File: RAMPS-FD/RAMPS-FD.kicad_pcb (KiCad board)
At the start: 2 copper layers, 100 x 100 mm, 159 parts, among them J1 NET-TIE, K201 S1, K202 S2, K203 S3, K204 S4, M101 LOGO_OSHW, P1 SERIAL1, P101 HB_IN, P102 RESET, P105 12V-AUX, P108 POWER_IN, P2 I2C-1, P201 3 2 1, P202 3 2 1, P203 3 2 1, P204 X, P205 Y, P206 Z1, P207 3 2 1, P208 3 2 1, P209 3 2 1, P210 E2, P211 I2C-0, P212 E1, P213 AUX-4, P214 AUX-2, P215 AUX-3, P216 SERIAL0, P217 E0, P218 D11, P219 EXT_5V, P3 Z2, P301 THERMISTORS, P302 ESTOP, P403 D9, P404 D8, P405 D10, P801 ENDSTOPS, P802 -X+ -Y+ -Z+, P901 D12, P902 D2, Q1 DMN2075, Q101 DMN2075, Q201 IRLB8743PBF, Q202 IRLB8743PBF, Q203 IRLB8743PBF, Q206 IRLB8743PBF, Q901 DMN2075U, Q902 DMN2075U, SW101 RESET, U1 74HCT125, U2 74HCT244, U201 X, U202 Y, U203 Z, U204 E2, U205 E1, U206 E0, U3 LM7812, U4 L7805CV-DG, U601 24C512, U801 74HC4050

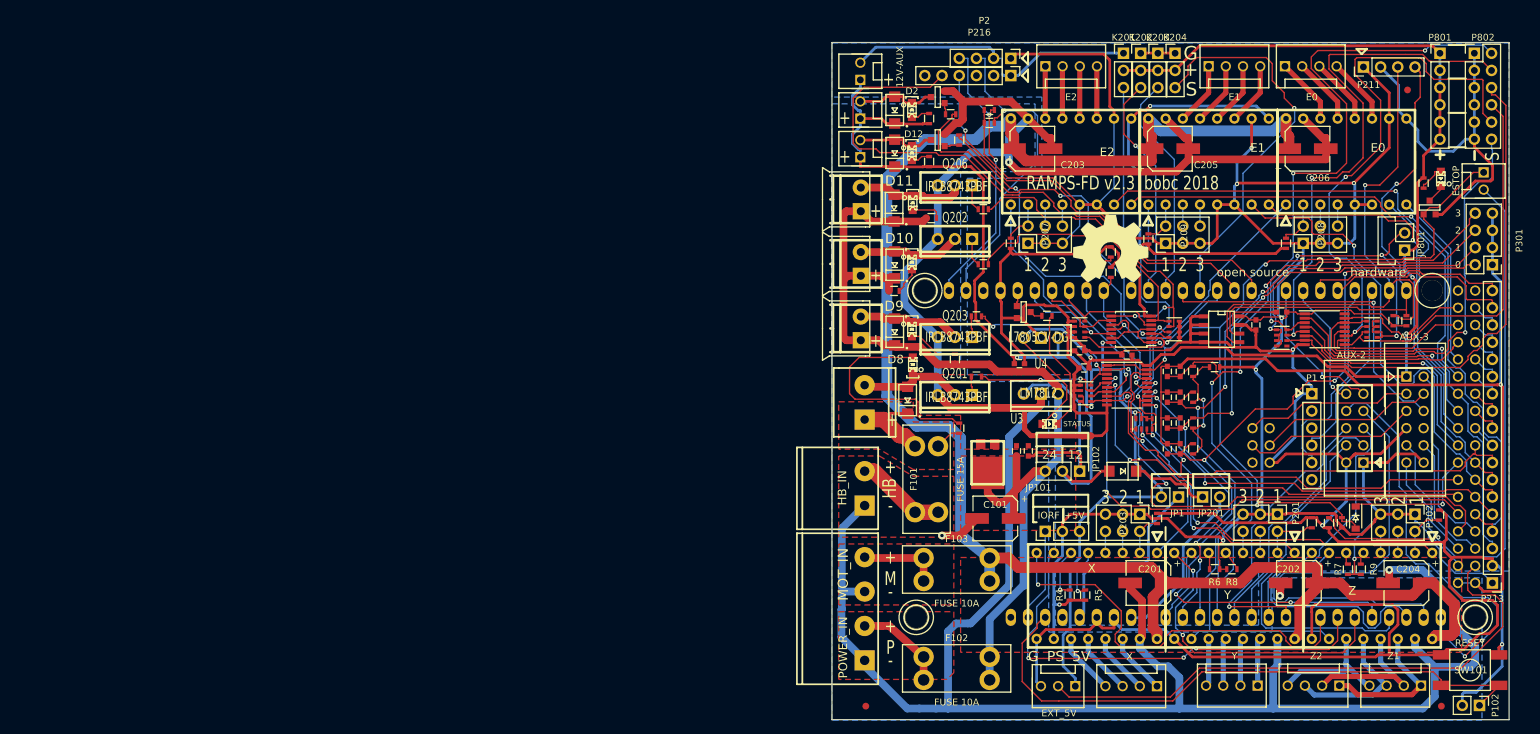
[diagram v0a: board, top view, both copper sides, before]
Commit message: Inital Commit RAMPS FD v2.3. SPI Support for every Driver added.
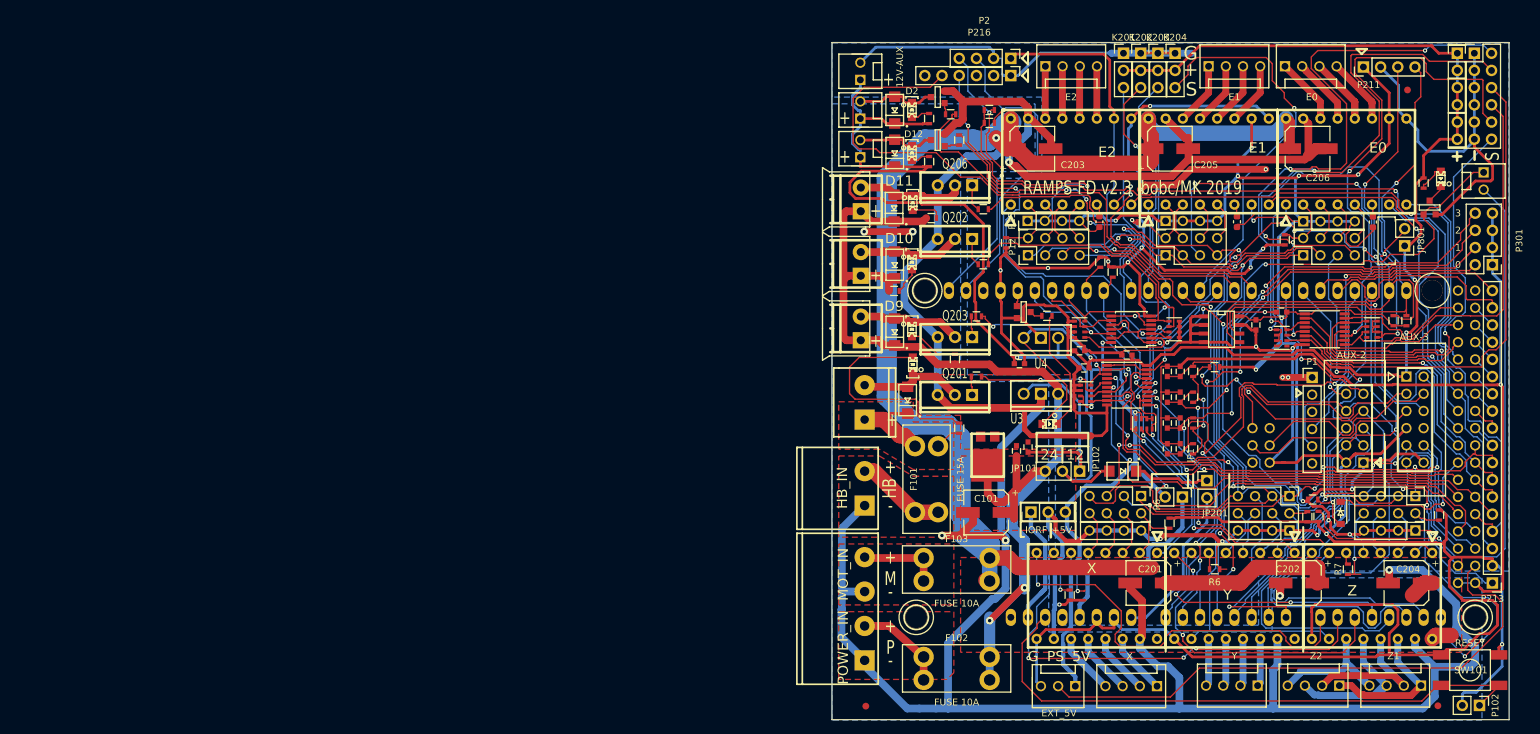
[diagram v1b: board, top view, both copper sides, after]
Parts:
- removed M101: LOGO_OSHW, rmc:OSHW_logo_2
- removed P201, P202, P203, P207, P208, P209: 3 2 1, Pin_Headers:Pin_Header_Straight_2x03_Pitch2.54mm
- removed R5, R8, R9: 10k, Resistors_SMD:R_0603
- added P10: THERMISTORS, Connector_PinHeader_2.54mm:PinHeader_2x04_P2.54mm_Vertical, F.Cu at (101.6, 71.0)
- added P11: THERMISTORS, Connector_PinHeader_2.54mm:PinHeader_2x04_P2.54mm_Vertical, F.Cu at (121.9, 71.0)
- added P12: THERMISTORS, Connector_PinHeader_2.54mm:PinHeader_2x04_P2.54mm_Vertical, F.Cu at (81.3, 71.0)
- added P13: I2C-0, Connector_PinHeader_2.54mm:PinHeader_1x04_P2.54mm_Vertical, F.Cu at (121.9, 66.0)
- added P14: I2C-0, Connector_PinHeader_2.54mm:PinHeader_1x04_P2.54mm_Vertical, F.Cu at (101.6, 65.9)
- added P15: I2C-0, Connector_PinHeader_2.54mm:PinHeader_1x04_P2.54mm_Vertical, F.Cu at (81.2, 65.9)
- added P4: THERMISTORS, Connector_PinHeader_2.54mm:PinHeader_2x04_P2.54mm_Vertical, F.Cu at (119.9, 106.6)
- added P5: THERMISTORS, Connector_PinHeader_2.54mm:PinHeader_2x04_P2.54mm_Vertical, F.Cu at (138.5, 106.6)
- added P6: THERMISTORS, Connector_PinHeader_2.54mm:PinHeader_2x04_P2.54mm_Vertical, F.Cu at (98.0, 106.5)
- added P7: I2C-0, Connector_PinHeader_2.54mm:PinHeader_1x04_P2.54mm_Vertical, F.Cu at (98.0, 111.6)
- added P8: I2C-0, Connector_PinHeader_2.54mm:PinHeader_1x04_P2.54mm_Vertical, F.Cu at (119.9, 111.6)
- added P9: I2C-0, Connector_PinHeader_2.54mm:PinHeader_1x04_P2.54mm_Vertical, F.Cu at (138.5, 111.6)
- added R10: 10k, Resistor_SMD:R_0603_1608Metric, F.Cu at (91.8, 66.0)
- added R12: 10k, Resistor_SMD:R_0603_1608Metric, F.Cu at (112.1, 66.0)
- added R14: 10k, Resistor_SMD:R_0603_1608Metric, F.Cu at (132.2, 66.1)
- U3: value LM7812 -> R-78E12-0.5
- moved R304 5.51 mm to (123.3, 107.1), turned to 0 degrees
- moved JP101 3.54 mm to (81.7, 108.9)
- moved R208 2.63 mm to (98.2, 66.1), turned to 180 degrees
- moved P801 2.57 mm to (144.7, 41.1)
- moved JP1 2.50 mm to (107.7, 104.3), turned to 0 degrees
- moved P1 2.41 mm to (123.2, 89.0)
- moved D301 2.33 mm to (127.4, 109.0)
- moved R402 2.16 mm to (91.9, 72.0)
- moved R202 1.97 mm to (102.2, 110.6)
- moved R305 1.81 mm to (124.2, 109.6)
- moved C101 1.61 mm to (75.1, 109.0)
- moved R203 1.11 mm to (122.5, 109.6), turned to 270 degrees
- moved D102 1.10 mm to (75.3, 100.5)
- moved R207 0.70 mm to (78.0, 69.2)
- moved JP801 0.63 mm to (136.9, 69.6)
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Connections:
- P1 pad 2: (no net) -> Net-(P1-Pad2)
- P1 pad 3: (no net) -> Net-(P1-Pad3)
- P1 pad 6: (no net) -> Net-(P1-Pad6)
- P215 pad 8: (no net) -> Net-(P215-Pad8)
- P216 pad 2: (no net) -> Net-(P216-Pad2)
- P216 pad 3: (no net) -> Net-(P216-Pad3)
- P216 pad 6: (no net) -> Net-(P216-Pad6)
- RP801 pad 1: (no net) -> Net-(RP801-Pad1)
- RP802 pad 4: (no net) -> Net-(RP802-Pad4)
- SHIELD101 pad 3V3: (no net) -> +3V3
- SHIELD101 pad 5V_4: (no net) -> Net-(SHIELD101-Pad5V_4)
- SHIELD101 pad 5V_5: (no net) -> Net-(SHIELD101-Pad5V_5)
- SHIELD101 pad 5V_6: (no net) -> Net-(SHIELD101-Pad5V_6)
- SHIELD101 pad AREF: (no net) -> Net-(SHIELD101-PadAREF)
- SHIELD101 pad RST2: (no net) -> Net-(SHIELD101-PadRST2)
- U201 pad 4: STEP_X_CS -> Net-(P6-Pad6)
- U202 pad 4: STEP_Y_CS -> Net-(P4-Pad6)
- U203 pad 4: STEP_Z_CS -> Net-(P5-Pad6)
- U204 pad 5: +V_LOGIC -> Net-(P12-Pad8)
- U204 pad 6: +V_LOGIC -> Net-(R10-Pad2)
- U205 pad 5: +V_LOGIC -> Net-(P10-Pad8)
- U205 pad 6: +V_LOGIC -> Net-(R12-Pad2)
- U206 pad 5: +V_LOGIC -> Net-(P11-Pad8)
- U206 pad 6: +V_LOGIC -> Net-(R14-Pad2)
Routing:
- net D50-MISO: track 18.4 -> 174.1 mm, vias 0 -> 5
- net D51-MOSI: track 19.3 -> 161.8 mm, vias 0 -> 6
- net D52-SCK: track 18.4 -> 159.3 mm, vias 0 -> 5
- net A5: track 31.2 -> 117.4 mm, vias 0 -> 3
- net AD14: track 68.5 -> 133.9 mm, vias 0 -> 6
- net AD15: track 61.4 -> 116.8 mm, vias 2 -> 6
- net +V_LOGIC: track 436.7 -> 480.6 mm, vias 8 -> 18
- net GND: track 604.7 -> 643.4 mm, vias 6 -> 18
- net A4: track 37.4 -> 74.3 mm, vias 0 -> 2
- net Net-(JP801-Pad2): track 57.5 -> 82.0 mm, vias 4 -> 3
- net +V_MOTOR: track 253.1 -> 231.9 mm, vias 0 -> 1
- net +12P: track 119.3 -> 138.7 mm
- net /Stepper Drivers/Z-1A: track 21.3 -> 36.9 mm
- net +5V: track 271.6 -> 287.0 mm
- net MOT_GND: track 430.1 -> 445.3 mm, vias 4 -> 7
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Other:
- board text added: "RAMPS-FD v2.3 bobc/MK 2019"
- board text removed: "RAMPS-FD v2.3 bobc 2018"

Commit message: Added UART for Communication with TMC2209 Drivers, improved inverse-polarity protection, added Driver Protection. Two Layer Design
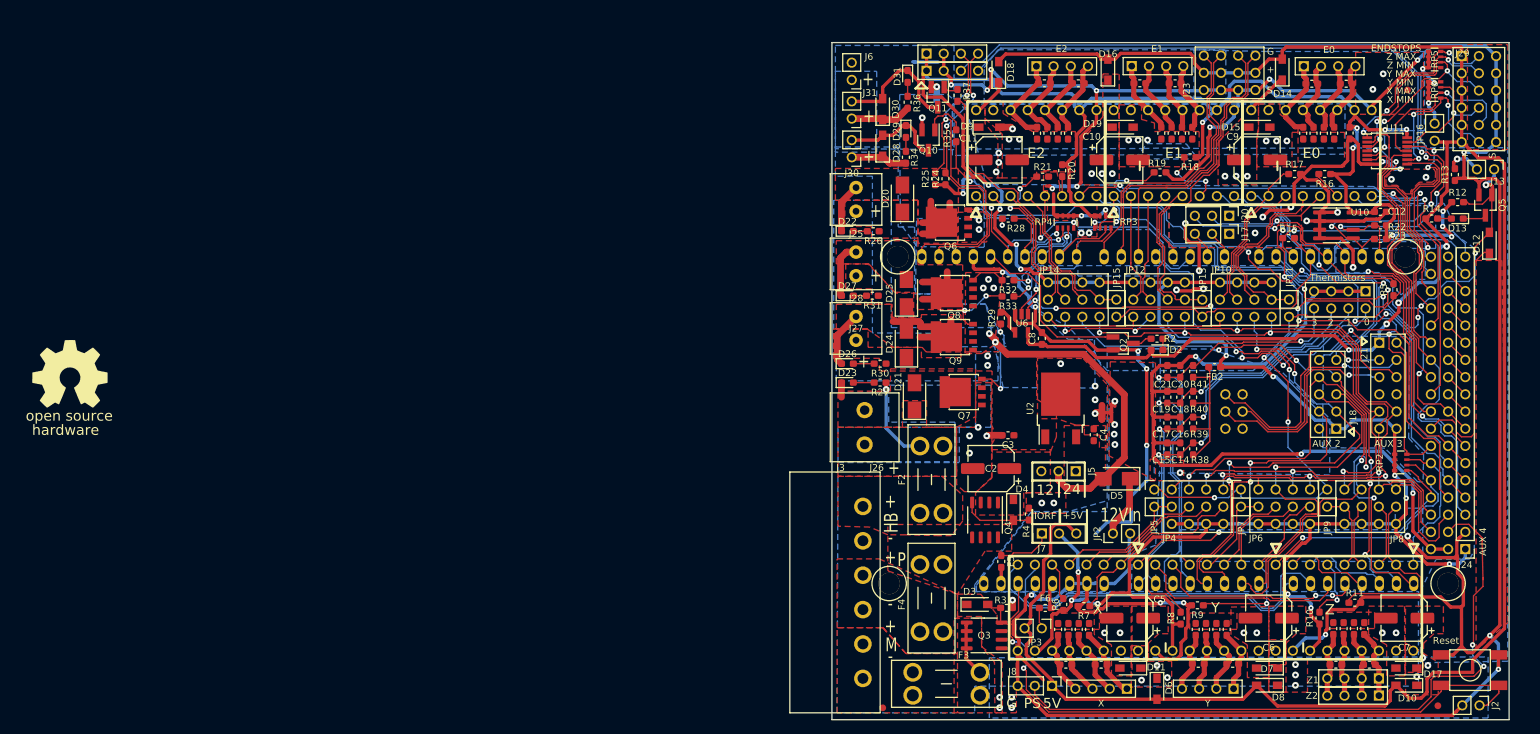
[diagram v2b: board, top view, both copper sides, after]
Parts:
- removed C102: 100n 50V, Capacitors_SMD:C_0603
- removed the C2 at (89.5, 87.6)
- removed C203: 100u 35V, Capacitors_SMD:CP_Elec_6.3x7.7
- removed D101: STATUS, rmc:LED-0805_GREEN
- removed D102: V10P10, rmc:TO277A_RMC
- removed D203, D902: LED RED, rmc:LED-0805_RED
- removed F102, F103: FUSE 10A, rmc:Keystone_3568
- removed J1: NET-TIE, rmc:TIE-1MM
- removed JP102: VSEL, Pin_Headers:Pin_Header_Straight_1x03_Pitch2.54mm
- removed JP201: 5V_SEL, Pin_Headers:Pin_Header_Straight_1x02_Pitch2.54mm
- removed K201: S1, Pin_Headers:Pin_Header_Straight_1x03_Pitch2.54mm
- removed K202: S2, Pin_Headers:Pin_Header_Straight_1x03_Pitch2.54mm
- removed K203: S3, Pin_Headers:Pin_Header_Straight_1x03_Pitch2.54mm
- removed K204: S4, Pin_Headers:Pin_Header_Straight_1x03_Pitch2.54mm
- removed P1: SERIAL1, Pin_Headers:Pin_Header_Straight_1x06_Pitch2.54mm
- removed P10, P11, P12, P4, P5, P6: THERMISTORS, Connector_PinHeader_2.54mm:PinHeader_2x04_P2.54mm_Vertical
- removed P101: HB_IN, w_conn_screw:mstba_2,5%2f2-g-5,08
- removed P108: POWER_IN, w_conn_screw:mstba_2,5%2f4-g-5,08
- removed P13, P14, P15, P7, P8, P9: I2C-0, Connector_PinHeader_2.54mm:PinHeader_1x04_P2.54mm_Vertical
- removed P204: X, rmc:CONN_KK_2.54_4W
- removed P216: SERIAL0, Pin_Headers:Pin_Header_Straight_1x06_Pitch2.54mm
- removed P301: THERMISTORS, Pin_Headers:Pin_Header_Straight_2x04_Pitch2.54mm
- removed P801: ENDSTOPS, Pin_Headers:Pin_Header_Straight_1x06_Pitch2.54mm
- removed P802: -X+ -Y+ -Z+, Pin_Headers:Pin_Header_Straight_2x06_Pitch2.54mm
- removed R101: 330R, Resistors_SMD:R_0603
- removed R219, R905, R906: 1k, Resistors_SMD:R_0603
- removed R401, R402: 10k, Resistors_SMD:R_0603
- removed the RP2 at (98.4, 95.9)
- removed SHIELD101: ARDUINO_DUE_SHIELD, rmc:ARDUINO_MEGA_DUE_SHIELD_FOOTPRINT_RMC
- removed the U2 at (95.9, 90.2)
- removed U204: E2, rmc:POLOLU
- removed U206: E0, rmc:POLOLU
- removed the U3 at (83.2, 91.4)
- removed the U4 at (83.2, 83.2)
- removed U601: 24C512, libcms:SO8E
- removed U801: 74HC4050, Housings_SSOP:TSSOP-16_4.4x5mm_Pitch0.65mm
- added D10: DS110W, RAMPS-FD:D_SOD-123F, F.Cu at (137.2, 134.5)
- added D11: SMF36CA, RAMPS-FD:D_SOD-123F, F.Cu at (96.4, 132.0)
- added D14: DS110W, RAMPS-FD:D_SOD-123F, F.Cu at (118.8, 43.6)
- added D15: SMF36CA, RAMPS-FD:D_SOD-123F, F.Cu at (115.4, 52.1)
- added D16: DS110W, RAMPS-FD:D_SOD-123F, F.Cu at (93.1, 43.6)
- added D17: SMF36CA, RAMPS-FD:D_SOD-123F, F.Cu at (137.2, 132.0)
- added D18: DS110W, RAMPS-FD:D_SOD-123F, F.Cu at (77.0, 43.9)
- added D19: SMF36CA, RAMPS-FD:D_SOD-123F, F.Cu at (95.2, 52.1)
- added D2: LED_0603_GREEN, RAMPS-FD:LED_0603, F.Cu at (100.3, 85.0)
- added D26: LED_0603_RED, RAMPS-FD:LED_0603, F.Cu at (54.6, 87.0)
- added D3: KDZVTR11B, RAMPS-FD:D_SOD-123F, F.Cu at (73.8, 122.6)
- added D31: LED_0603_RED, RAMPS-FD:LED_0603, F.Cu at (63.5, 44.6)
- added D4: KDZVTR11B, RAMPS-FD:D_SOD-123F, F.Cu at (79.1, 108.6)
- added D6: DS110W, RAMPS-FD:D_SOD-123F, F.Cu at (100.3, 135.0)
- added D7: SMF36CA, RAMPS-FD:D_SOD-123F, F.Cu at (116.6, 132.0)
- added D8: DS110W, RAMPS-FD:D_SOD-123F, F.Cu at (116.6, 134.5)
- added D9: SMF36CA, RAMPS-FD:D_SOD-123F, F.Cu at (75.6, 52.1)
- added F3: Keystone_3568, RAMPS-FD:Fuseholder_Blade_Mini_Keystone_3568, F.Cu at (64.3, 132.6)
- added F4: Keystone_3568, RAMPS-FD:Fuseholder_Blade_Mini_Keystone_3568, F.Cu at (65.3, 126.6)
- added F5: FUSE_750mA_0603, RAMPS-FD:R_0603, F.Cu at (77.3, 116.2)
- added F6: FUSE_750mA_0603, RAMPS-FD:R_0603, F.Cu at (83.8, 123.1)
- added J17: 1x3PinHeader, RAMPS-FD:PinHeader_1x03_P2.54mm_Vertical, F.Cu at (111.0, 67.8)
- added J20: 1x3PinHeader, RAMPS-FD:PinHeader_1x03_P2.54mm_Vertical, F.Cu at (111.0, 65.2)
- added J23: 3x4PinHeader, RAMPS-FD:4x3_2.54mm_Header, F.Cu at (107.2, 46.6)
- added J29: 3x6PinHeader, RAMPS-FD:6x3_2.54mm_Header, F.Cu at (145.3, 41.6)
- added J3: 6_PinScrewPlugableTerminal_P508, RAMPS-FD:6x1_P508_RA, F.Cu at (56.9, 120.8)
- added J32: 2x4PinHeader_2.54mm, RAMPS-FD:pin_header_2.54mm_2x4, F.Cu at (127.3, 77.6)
- added J5: 1x3JumperArray, RAMPS-FD:PinHeader_1x03_P2.54mm_Vertical, F.Cu at (88.3, 102.9)
- added J9: 1x4PinHeader, RAMPS-FD:pin_header_2.54mm_1x4, F.Cu at (92.1, 135.0)
- added JP10: 4x3JumperArray, RAMPS-FD:4x3_2.54mm_Header, F.Cu at (109.6, 80.1)
- added JP11: 1x2JumperArray, RAMPS-FD:PinHeader_1x02_P2.54mm_Vertical, F.Cu at (119.8, 80.1)
- added JP12: 4x3JumperArray, RAMPS-FD:4x3_2.54mm_Header, F.Cu at (96.8, 80.1)
- added JP13: 1x2JumperArray, RAMPS-FD:PinHeader_1x02_P2.54mm_Vertical, F.Cu at (107.0, 80.1)
- added JP14: 4x3JumperArray, RAMPS-FD:4x3_2.54mm_Header, F.Cu at (84.2, 80.1)
- added JP15: 1x2JumperArray, RAMPS-FD:PinHeader_1x02_P2.54mm_Vertical, F.Cu at (94.3, 80.1)
- added JP3: 1x2JumperArray, RAMPS-FD:PinHeader_1x02_P2.54mm_Vertical, F.Cu at (83.3, 126.1)
- added JP4: 4x3JumperArray, RAMPS-FD:4x3_2.54mm_Header, F.Cu at (110.1, 105.6)
- added JP5: 1x2JumperArray, RAMPS-FD:PinHeader_1x02_P2.54mm_Vertical, F.Cu at (99.9, 105.6)
- added JP6: 4x3JumperArray, RAMPS-FD:4x3_2.54mm_Header, F.Cu at (122.9, 105.6)
- added JP7: 1x2JumperArray, RAMPS-FD:PinHeader_1x02_P2.54mm_Vertical, F.Cu at (112.7, 105.6)
- added JP8: 4x3JumperArray, RAMPS-FD:4x3_2.54mm_Header, F.Cu at (135.6, 105.6)
- added JP9: 1x2JumperArray, RAMPS-FD:PinHeader_1x02_P2.54mm_Vertical, F.Cu at (125.5, 105.6)
- added M2: LOGO_OSHW, RAMPS-FD:OSHW_logo_2, F.Cu at (-60.2, 88.5)
- added NT1: NetTie-2_SMD_Pad0.5mm, NetTie:NetTie-2_SMD_Pad0.5mm, F.Cu at (93.1, 94.2)
- added Q3: TDM3415, RAMPS-FD:SO-8_3.9x4.9mm_P1.27mm, F.Cu at (74.8, 127.1)
- added Q4: TDM3415, RAMPS-FD:SO-8_3.9x4.9mm_P1.27mm, F.Cu at (74.9, 110.1)
- added R14: 330R, RAMPS-FD:R_0603, F.Cu at (140.9, 65.6)
- added R15: 1k, RAMPS-FD:R_0603, F.Cu at (119.8, 68.5)
- added R2: 330R, RAMPS-FD:R_0603, F.Cu at (100.3, 83.3)
- added R27: 1k, RAMPS-FD:R_0603, F.Cu at (59.4, 89.8)
- added R34: 1k, RAMPS-FD:R_0603, F.Cu at (63.2, 56.5)
- added R36: 1k, RAMPS-FD:R_0603, F.Cu at (63.5, 48.4)
- added R5: 1k, RAMPS-FD:R_0603, F.Cu at (135.3, 76.1)
- added R6: 10k, RAMPS-FD:R_0603, F.Cu at (86.5, 122.6)
- added REF**: OSHW-Logo2_9.8x8mm_SilkScreen, Symbol:OSHW-Logo2_9.8x8mm_SilkScreen, B.Cu at (81.9, 88.5)
- added SHIELD2: ARDUINO_DUE_SHIELD, RAMPS-FD:ARDUINO_MEGA_DUE_SHIELD_FOOTPRINT_RMC, F.Cu at (46.8, 122.0)
- added U10: 24C512, RAMPS-FD:SOIC-8_3.9x4.9mm_P1.27mm, F.Cu at (126.8, 66.6)
- added U11: MC74LCX07, RAMPS-FD:TSSOP-14_4.4x5mm_P0.65mm, F.Cu at (134.3, 55.6)
- added U6: SN74LV1T125, RAMPS-FD:SOT-23-5, F.Cu at (80.3, 81.0)
- added U7: Pololu, RAMPS-FD:POLOLU, F.Cu at (123.1, 55.9)
- added U9: Pololu, RAMPS-FD:POLOLU, F.Cu at (82.5, 55.9)
- added VR10: 33V, RAMPS-FD:R_0603, F.Cu at (107.6, 126.2)
- added VR11: 33V, RAMPS-FD:R_0603, F.Cu at (106.0, 126.2)
- added VR12: 33V, RAMPS-FD:R_0603, F.Cu at (111.5, 131.3)
- added VR13: 33V, RAMPS-FD:R_0603, F.Cu at (106.4, 131.3)
- added VR14: 33V, RAMPS-FD:R_0603, F.Cu at (129.4, 126.1)
- added VR15: 33V, RAMPS-FD:R_0603, F.Cu at (130.9, 126.1)
- added VR16: 33V, RAMPS-FD:R_0603, F.Cu at (127.9, 126.1)
- added VR17: 33V, RAMPS-FD:R_0603, F.Cu at (126.4, 126.1)
- added VR18: 33V, RAMPS-FD:R_0603, F.Cu at (131.7, 131.4)
- added VR19: 33V, RAMPS-FD:R_0603, F.Cu at (126.7, 131.4)
- added VR2: 33V, RAMPS-FD:R_0603, F.Cu at (92.1, 131.4)
- added VR20: 33V, RAMPS-FD:R_0603, F.Cu at (123.2, 45.7)
- added VR21: 33V, RAMPS-FD:R_0603, F.Cu at (128.3, 45.7)
- added VR22: 33V, RAMPS-FD:R_0603, F.Cu at (123.4, 53.0)
- added VR23: 33V, RAMPS-FD:R_0603, F.Cu at (121.9, 53.0)
- added VR24: 33V, RAMPS-FD:R_0603, F.Cu at (125.0, 53.0)
- added VR25: 33V, RAMPS-FD:R_0603, F.Cu at (126.5, 53.0)
- added VR26: 33V, RAMPS-FD:R_0603, F.Cu at (97.8, 45.6)
- added VR27: 33V, RAMPS-FD:R_0603, F.Cu at (103.0, 45.6)
- added VR28: 33V, RAMPS-FD:R_0603, F.Cu at (101.0, 53.0)
- added VR29: 33V, RAMPS-FD:R_0603, F.Cu at (102.5, 53.0)
- added VR3: 33V, RAMPS-FD:R_0603, F.Cu at (86.9, 131.4)
- added VR30: 33V, RAMPS-FD:R_0603, F.Cu at (104.0, 53.0)
- added VR31: 33V, RAMPS-FD:R_0603, F.Cu at (105.5, 53.0)
- added VR32: 33V, RAMPS-FD:R_0603, F.Cu at (82.6, 53.0)
- added VR33: 33V, RAMPS-FD:R_0603, F.Cu at (84.1, 53.0)
- added VR34: 33V, RAMPS-FD:R_0603, F.Cu at (85.7, 53.0)
- added VR35: 33V, RAMPS-FD:R_0603, F.Cu at (87.2, 53.0)
- added VR36: 33V, RAMPS-FD:R_0603, F.Cu at (83.7, 45.6)
- added VR37: 33V, RAMPS-FD:R_0603, F.Cu at (88.7, 45.6)
- added VR4: 33V, RAMPS-FD:R_0603, F.Cu at (88.8, 126.2)
- added VR5: 33V, RAMPS-FD:R_0603, F.Cu at (90.3, 126.2)
- added VR6: 33V, RAMPS-FD:R_0603, F.Cu at (87.2, 126.2)
- added VR7: 33V, RAMPS-FD:R_0603, F.Cu at (85.7, 126.2)
- added VR8: 33V, RAMPS-FD:R_0603, F.Cu at (109.1, 126.2)
- added VR9: 33V, RAMPS-FD:R_0603, F.Cu at (110.6, 126.2)
- C10: renamed from C205; value 100u 35V -> 100u_35V; footprint Capacitors_SMD:CP_Elec_6.3x7.7 -> RAMPS-FD:CP_Elec_6.3x7.7
- C11: renamed from C204; value 100u 35V -> 100u_35V; footprint Capacitors_SMD:CP_Elec_6.3x7.7 -> RAMPS-FD:CP_Elec_6.3x7.7
- C12: renamed from C601; footprint Capacitors_SMD:C_0603 -> RAMPS-FD:C_0603
- C13: renamed from C305; footprint Capacitors_SMD:C_0603 -> RAMPS-FD:C_0603
- C14: renamed from C504; footprint Capacitors_SMD:C_0603 -> RAMPS-FD:C_0603
- C15: renamed from C301; footprint Capacitors_SMD:C_0603 -> RAMPS-FD:C_0603
- C16: renamed from C505; footprint Capacitors_SMD:C_0603 -> RAMPS-FD:C_0603
- C17: renamed from C302; footprint Capacitors_SMD:C_0603 -> RAMPS-FD:C_0603
- C18: renamed from C503; footprint Capacitors_SMD:C_0603 -> RAMPS-FD:C_0603
- C19: renamed from C303; footprint Capacitors_SMD:C_0603 -> RAMPS-FD:C_0603
- C2: renamed from C101; value 100u 35V -> 100u_35V; footprint Capacitors_SMD:CP_Elec_6.3x7.7 -> RAMPS-FD:CP_Elec_6.3x7.7
- C20: renamed from C502; footprint Capacitors_SMD:C_0603 -> RAMPS-FD:C_0603
- C21: renamed from C501; footprint Capacitors_SMD:C_0603 -> RAMPS-FD:C_0603
- C3: footprint Capacitors_SMD:C_0603 -> RAMPS-FD:C_0603
- C4: renamed from C207; footprint Capacitors_SMD:C_0603 -> RAMPS-FD:C_0603
- C5: renamed from C201; value 100u 35V -> 100u_35V; footprint Capacitors_SMD:CP_Elec_6.3x7.7 -> RAMPS-FD:CP_Elec_6.3x7.7
- C6: renamed from C202; value 100u 35V -> 100u_35V; footprint Capacitors_SMD:CP_Elec_6.3x7.7 -> RAMPS-FD:CP_Elec_6.3x7.7
- C7: renamed from C4; value 100n -> 100u_35V; footprint Capacitors_SMD:C_0603 -> RAMPS-FD:CP_Elec_6.3x7.7
- C8: renamed from C1; footprint Capacitors_SMD:C_0603 -> RAMPS-FD:C_0603
- C9: renamed from C206; value 100u 35V -> 100u_35V; footprint Capacitors_SMD:CP_Elec_6.3x7.7 -> RAMPS-FD:CP_Elec_6.3x7.7
- D12: renamed from D301; value 1N4148 -> 2CZ4007; footprint Diodes_SMD:SOD-123 -> RAMPS-FD:D_SOD-123F
- D13: renamed from D1; value ESTOP -> LED_0603_GREEN; footprint rmc:LED-0805_GREEN -> RAMPS-FD:LED_0603
- D20: renamed from D403; value ES1F -> MRA4003T3G; footprint rmc:DO-214AC -> RAMPS-FD:D_SMA
- D21: renamed from D404; value ES1F -> MRA4003T3G; footprint rmc:DO-214AC -> RAMPS-FD:D_SMA
- D22: renamed from D204; value LED RED -> LED_0603_RED; footprint rmc:LED-0805_RED -> RAMPS-FD:LED_0603
- D23: renamed from D201; value LED RED -> LED_0603_RED; footprint rmc:LED-0805_RED -> RAMPS-FD:LED_0603
- D24: renamed from D401; value ES1F -> MRA4003T3G; footprint rmc:DO-214AC -> RAMPS-FD:D_SMA
- D25: renamed from D402; value ES1F -> MRA4003T3G; footprint rmc:DO-214AC -> RAMPS-FD:D_SMA
- D27: renamed from D202; value LED RED -> LED_0603_RED; footprint rmc:LED-0805_RED -> RAMPS-FD:LED_0603
- D28: renamed from D903; value ES1F -> 2CZ4007; footprint rmc:DO-214AC -> RAMPS-FD:D_SOD-123F
- D29: renamed from D901; value LED RED -> LED_0603_RED; footprint rmc:LED-0805_RED -> RAMPS-FD:LED_0603
- D30: renamed from D904; value ES1F -> 2CZ4007; footprint rmc:DO-214AC -> RAMPS-FD:D_SOD-123F
- D5: renamed from D103; value ES1F -> MRA4003T3G; footprint rmc:DO-214AC -> RAMPS-FD:D_SMA
- F2: renamed from F101; value FUSE 15A -> Keystone_3568; footprint rmc:Keystone_3568 -> RAMPS-FD:Fuseholder_Blade_Mini_Keystone_3568
- FB2: renamed from L1; value FB -> FB0603; footprint Resistors_SMD:R_0603 -> RAMPS-FD:R_0603
- FID2: renamed from FID1; footprint Fiducials:Fiducial_1mm_Dia_2.54mm_Outer_CopperTop -> RAMPS-FD:Fiducial_1mm_Mask2mm
- FID3: renamed from FID2; footprint Fiducials:Fiducial_1mm_Dia_2.54mm_Outer_CopperTop -> RAMPS-FD:Fiducial_1mm_Mask2mm
- FID4: renamed from FID3; footprint Fiducials:Fiducial_1mm_Dia_2.54mm_Outer_CopperTop -> RAMPS-FD:Fiducial_1mm_Mask2mm
- J10: renamed from P205; value Y -> 1x4PinHeader; footprint rmc:CONN_KK_2.54_4W -> RAMPS-FD:pin_header_2.54mm_1x4
- J11: renamed from P206; value Z1 -> 1x4PinHeader; footprint rmc:CONN_KK_2.54_4W -> RAMPS-FD:pin_header_2.54mm_1x4
- J12: renamed from P3; value Z2 -> 1x4PinHeader; footprint rmc:CONN_KK_2.54_4W -> RAMPS-FD:pin_header_2.54mm_1x4
- J13: renamed from P302; value ESTOP -> 2x1PinHeader; footprint rmc:CONN_KK_2.54_2W -> RAMPS-FD:PinHeader_1x02_P2.54mm_Vertical
- J14: renamed from P217; value E0 -> 1x4PinHeader; footprint rmc:CONN_KK_2.54_4W -> RAMPS-FD:pin_header_2.54mm_1x4
- J15: renamed from P212; value E1 -> 1x4PinHeader; footprint rmc:CONN_KK_2.54_4W -> RAMPS-FD:pin_header_2.54mm_1x4
- J16: renamed from P210; value E2 -> 1x4PinHeader; footprint rmc:CONN_KK_2.54_4W -> RAMPS-FD:pin_header_2.54mm_1x4
- J18: renamed from P214; value AUX-2 -> 2x5PinHeader; footprint rmc:PIN_ARRAY_5x2_RMC -> RAMPS-FD:pin_header_2.54mm_2x5
- J19: renamed from P211; value I2C-0 -> 1x4PinHeader; footprint Pin_Headers:Pin_Header_Straight_1x04_Pitch2.54mm -> RAMPS-FD:pin_header_2.54mm_1x4
- J2: renamed from P102; value RESET -> 2x1PinHeader; footprint Pin_Headers:Pin_Header_Straight_1x02_Pitch2.54mm -> RAMPS-FD:PinHeader_1x02_P2.54mm_Vertical
- J21: renamed from P215; value AUX-3 -> 2x6PinHeader; footprint rmc:PIN_ARRAY_6x2_RMC -> RAMPS-FD:pin_header_2.54mm_2x6
- J22: renamed from P2; value I2C-1 -> 1x4PinHeader; footprint Pin_Headers:Pin_Header_Straight_1x04_Pitch2.54mm -> RAMPS-FD:pin_header_2.54mm_1x4
- J24: renamed from P213; value AUX-4 -> 1x18PinHeader; footprint Pin_Headers:Pin_Header_Straight_1x18_Pitch2.54mm -> RAMPS-FD:PinHeader_1x18_P2.54mm_Vertical
- J25: renamed from P218; value D11 -> 2_PinScrewTerminal_P350; footprint rmc:RMC-pt_1,5-2-3,5-h -> RAMPS-FD:2x1_P350
- J26: renamed from P404; value D8 -> 2_PinScrewTerminal_P508; footprint w_conn_screw:mors_2p -> RAMPS-FD:2x1_P508
- J27: renamed from P403; value D9 -> 2_PinScrewTerminal_P350; footprint rmc:RMC-pt_1,5-2-3,5-h -> RAMPS-FD:2x1_P350
- J28: renamed from P405; value D10 -> 2_PinScrewTerminal_P350; footprint rmc:RMC-pt_1,5-2-3,5-h -> RAMPS-FD:2x1_P350
- J30: renamed from P901; value D12 -> 2x1PinHeader; footprint rmc:CONN_KK_2.54_2W -> RAMPS-FD:PinHeader_1x02_P2.54mm_Vertical
- J31: renamed from P902; value D2 -> 2x1PinHeader; footprint rmc:CONN_KK_2.54_2W -> RAMPS-FD:PinHeader_1x02_P2.54mm_Vertical
- J6: renamed from P105; value 12V-AUX -> 2x1PinHeader; footprint rmc:CONN_KK_2.54_2W -> RAMPS-FD:PinHeader_1x02_P2.54mm_Vertical
- J7: renamed from JP101; value VLOG -> 1x3JumperArray; footprint Pin_Headers:Pin_Header_Straight_1x03_Pitch2.54mm -> RAMPS-FD:PinHeader_1x03_P2.54mm_Vertical
- J8: renamed from P219; value EXT_5V -> 1x3PinHeader; footprint rmc:CONN_KK_2.54_3W -> RAMPS-FD:PinHeader_1x03_P2.54mm_Vertical
- JP16: renamed from JP801; value PULLUPS -> 1x2JumperArray; footprint Pin_Headers:Pin_Header_Straight_1x02_Pitch2.54mm -> RAMPS-FD:PinHeader_1x02_P2.54mm_Vertical
- JP2: renamed from JP1; value VIN -> 1x2JumperArray; footprint Pin_Headers:Pin_Header_Straight_1x02_Pitch2.54mm -> RAMPS-FD:PinHeader_1x02_P2.54mm_Vertical
- Q10: renamed from Q901; value DMN2075U -> NCE3416; footprint libcms:SOT23GDS -> RAMPS-FD:SOT-23
- Q11: renamed from Q902; value DMN2075U -> NCE3416; footprint libcms:SOT23GDS -> RAMPS-FD:SOT-23
- Q2: renamed from Q101; value DMN2075 -> NCE3416; footprint libcms:SOT23GDS -> RAMPS-FD:SOT-23
- Q5: renamed from Q1; value DMN2075 -> NCE3416; footprint libcms:SOT23GDS -> RAMPS-FD:SOT-23
- Q6: renamed from Q206; value IRLB8743PBF -> PSMN7R5-60YLX; footprint rmc:TO-220AB_IRF2804_RMC -> RAMPS-FD:LFPAK56
- Q7: renamed from Q201; value IRLB8743PBF -> PSMN1R8-40YLC; footprint rmc:TO-220AB_IRF2804_RMC -> RAMPS-FD:LFPAK56
- Q8: renamed from Q202; value IRLB8743PBF -> PSMN7R5-60YLX; footprint rmc:TO-220AB_IRF2804_RMC -> RAMPS-FD:LFPAK56
- Q9: renamed from Q203; value IRLB8743PBF -> PSMN7R5-60YLX; footprint rmc:TO-220AB_IRF2804_RMC -> RAMPS-FD:LFPAK56
- R10: renamed from R7; footprint Resistors_SMD:R_0603 -> RAMPS-FD:R_0603
- R11: renamed from R201; footprint Resistors_SMD:R_0603 -> RAMPS-FD:R_0603
- R12: renamed from R304; footprint Resistors_SMD:R_0603 -> RAMPS-FD:R_0603
- R13: renamed from R305; footprint Resistors_SMD:R_0603 -> RAMPS-FD:R_0603
- R16: renamed from R14; footprint Resistor_SMD:R_0603_1608Metric -> RAMPS-FD:R_0603
- R17: renamed from R210; footprint Resistors_SMD:R_0603 -> RAMPS-FD:R_0603
- R18: renamed from R12; footprint Resistor_SMD:R_0603_1608Metric -> RAMPS-FD:R_0603
- R19: renamed from R208; footprint Resistors_SMD:R_0603 -> RAMPS-FD:R_0603
- R20: renamed from R10; footprint Resistor_SMD:R_0603_1608Metric -> RAMPS-FD:R_0603
- R21: renamed from R207; footprint Resistors_SMD:R_0603 -> RAMPS-FD:R_0603
- R22: renamed from R211; value NF -> 10k; footprint Resistors_SMD:R_0603 -> RAMPS-FD:R_0603
- R23: renamed from R212; value NF -> 10k; footprint Resistors_SMD:R_0603 -> RAMPS-FD:R_0603
- R24: renamed from R1; value NF -> 10k; footprint Resistors_SMD:R_0603 -> RAMPS-FD:R_0603
- R25: renamed from R2; value NF -> 10k; footprint Resistors_SMD:R_0603 -> RAMPS-FD:R_0603
- R26: renamed from R222; footprint Resistors_SMD:R_0603 -> RAMPS-FD:R_0603
- R28: renamed from R703; value 220R -> 33R; footprint Resistors_SMD:R_0603 -> RAMPS-FD:R_0603
- R29: renamed from R701; value 220R -> 33R; footprint Resistors_SMD:R_0603 -> RAMPS-FD:R_0603
- R3: value 330R -> 10k; footprint Resistors_SMD:R_0603 -> RAMPS-FD:R_0603
- R30: renamed from R221; footprint Resistors_SMD:R_0603 -> RAMPS-FD:R_0603
- R31: renamed from R220; footprint Resistors_SMD:R_0603 -> RAMPS-FD:R_0603
- R32: renamed from R704; value 220R -> 33R; footprint Resistors_SMD:R_0603 -> RAMPS-FD:R_0603
- R33: renamed from R702; value 220R -> 33R; footprint Resistors_SMD:R_0603 -> RAMPS-FD:R_0603
- R35: renamed from R902; value 220R -> 33R; footprint Resistors_SMD:R_0603 -> RAMPS-FD:R_0603
- R37: renamed from R901; value 220R -> 33R; footprint Resistors_SMD:R_0603 -> RAMPS-FD:R_0603
- R38: renamed from R301; footprint Resistors_SMD:R_0603 -> RAMPS-FD:R_0603
- R39: renamed from R302; footprint Resistors_SMD:R_0603 -> RAMPS-FD:R_0603
- R4: footprint Resistors_SMD:R_0603 -> RAMPS-FD:R_0603
- R40: renamed from R303; footprint Resistors_SMD:R_0603 -> RAMPS-FD:R_0603
- R41: renamed from R501; footprint Resistors_SMD:R_0603 -> RAMPS-FD:R_0603
- R7: renamed from R202; footprint Resistors_SMD:R_0603 -> RAMPS-FD:R_0603
- R8: renamed from R6; footprint Resistors_SMD:R_0603 -> RAMPS-FD:R_0603
- R9: renamed from R203; footprint Resistors_SMD:R_0603 -> RAMPS-FD:R_0603
- RP2: renamed from RP1; value 10k -> 10kArrayx4; footprint Resistors_SMD:R_Cat16-4 -> RAMPS-FD:R_Array_Convex_4x0603
- RP3: value 10k -> 10kArrayx4; footprint Resistors_SMD:R_Cat16-4 -> RAMPS-FD:R_Array_Convex_4x0603
- RP4: renamed from RP401; value 10k -> 10kArrayx4; footprint Resistors_SMD:R_Cat16-4 -> RAMPS-FD:R_Array_Convex_4x0603
- RP5: renamed from RP801; value 10k -> 10kArrayx4; footprint Resistors_SMD:R_Cat16-4 -> RAMPS-FD:R_Array_Convex_4x0603
- RP6: renamed from RP802; value 10k -> 10kArrayx4; footprint Resistors_SMD:R_Cat16-4 -> RAMPS-FD:R_Array_Convex_4x0603
- SW2: renamed from SW101; value RESET -> PushButton; footprint rmc:SW_6x6_SMD -> RAMPS-FD:SW_6x6_SMD
- U2: renamed from U1; value 74HCT125 -> AS7812ADTR; footprint Housings_SSOP:TSSOP-14_4.4x5mm_Pitch0.65mm -> RAMPS-FD:TO-252-2
- U3: renamed from U201; value X -> Pololu; footprint rmc:POLOLU -> RAMPS-FD:POLOLU
- U4: renamed from U202; value Y -> Pololu; footprint rmc:POLOLU -> RAMPS-FD:POLOLU
- U5: renamed from U203; value Z -> Pololu; footprint rmc:POLOLU -> RAMPS-FD:POLOLU
- U8: renamed from U205; value E1 -> Pololu; footprint rmc:POLOLU -> RAMPS-FD:POLOLU
- moved R3 87.9 mm to (78.1, 123.1), turned to 0 degrees
- moved C11 86.7 mm to (77.0, 56.9), turned to 0 degrees
- moved J19 60.7 mm to (70.1, 43.7), turned to 0 degrees
- moved C7 56.4 mm to (136.8, 124.6)
- moved R13 54.3 mm to (144.3, 59.1)
- moved R12 48.9 mm to (144.7, 63.1)
- moved RP5 46.9 mm to (141.3, 42.1), turned to 180 degrees
- moved D12 45.5 mm to (149.4, 69.2), turned to 90 degrees
- moved RP2 38.8 mm to (136.3, 101.6), turned to 180 degrees
- moved RP6 36.5 mm to (141.3, 46.6)
- moved C13 28.3 mm to (128.8, 52.9), turned to 270 degrees
- moved RP3 25.4 mm to (92.3, 66.1), turned to 90 degrees
- moved C12 24.8 mm to (133.3, 64.6), turned to 0 degrees
- moved R9 20.8 mm to (106.3, 122.7), turned to 180 degrees
- moved R11 18.0 mm to (129.5, 122.3), turned to 0 degrees
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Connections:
- C3 pad 1: +12P -> +V_POWER
- C3 pad 2: GND -> MOT_GND
- C7 pad 1: +5V -> +V_MOTOR
- C7 pad 2: GND -> MOT_GND
- D12 pad 2: Net-(D301-Pad2) -> Net-(D12-Pad2)
- D13 pad 1: Net-(D1-Pad1) -> Net-(D13-Pad1)
- D13 pad 2: Net-(D1-Pad2) -> Net-(D13-Pad2)
- J13 pad 1: Net-(D301-Pad2) -> Net-(D12-Pad2)
- J24 pad 5: D45 -> /E2_EN_BUF
- J24 pad 8: D39 -> /E1_EN_BUF
- J7 pad 1: IOREF -> Net-(F5-Pad1)
- R12 pad 2: Net-(D301-Pad2) -> Net-(D12-Pad2)
- R28 pad 1: FET4_BUF -> D11-FET4
- R28 pad 2: Net-(Q206-PadG) -> Net-(Q6-Pad4)
- R29 pad 2: Net-(Q201-PadG) -> Net-(Q7-Pad4)
- R3 pad 1: +5V -> Net-(D3-Pad2)
- R3 pad 2: Net-(D1-Pad2) -> MOT_GND
- R32 pad 1: D10_BUF -> D10
- R32 pad 2: Net-(Q202-PadG) -> Net-(Q8-Pad4)
- R33 pad 1: D9_BUF -> D9
- R33 pad 2: Net-(Q203-PadG) -> Net-(Q9-Pad4)
- R35 pad 1: FET5_BUF -> D12-FET5
- R35 pad 2: Net-(Q901-PadG) -> Net-(Q10-Pad1)
- R37 pad 1: FET6_BUF -> D2-FET6
- R37 pad 2: Net-(Q902-PadG) -> Net-(Q11-Pad1)
- R4 pad 1: +V_LOGIC -> Net-(D4-Pad2)
- R4 pad 2: Net-(R4-Pad2) -> MOT_GND
- RP2 pad 1: GND -> /X_EN_BUF
- RP2 pad 2: GND -> /Y_EN_BUF
- RP2 pad 3: GND -> /Z_EN_BUF
- RP2 pad 4: GND -> /E0_EN_BUF
- RP2 pad 5: D10_BUF -> +V_LOGIC
- RP2 pad 6: FET4_BUF -> +V_LOGIC
- RP2 pad 7: FET5_BUF -> +V_LOGIC
- RP2 pad 8: FET6_BUF -> +V_LOGIC
- RP3 pad 3: D8_BUF -> D9
- RP3 pad 4: D9_BUF -> D8
- RP3 pad 7: +5V -> +V_LOGIC
- RP3 pad 8: +5V -> +V_LOGIC
- RP4 pad 5: D2-FET6 -> D12-FET5
- RP4 pad 6: D12-FET5 -> D11-FET4
- RP4 pad 7: D11-FET4 -> D10
- RP4 pad 8: D10 -> D2-FET6
- U2 pad 1: Net-(D301-Pad2) -> +V_POWER
- U2 pad 2: D2-FET6 -> MOT_GND
- U2 pad 3: FET6_BUF -> /Power/LP_2
- U3 pad 6: Net-(R4-Pad2) -> Net-(R6-Pad2)
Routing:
- net MOT_GND: track 445.3 -> 14.3 mm, vias 7 -> 33
- net +V_MOTOR: track 231.9 -> 12.6 mm, vias 1 -> 24
- net +V_POWER: track 156.4 -> 0.00 mm
- net Net-(D301-Pad2): track 143.0 -> 0.00 mm, vias 6 -> 0
- net Net-(D12-Pad2): track 0.00 -> 102.1 mm, vias 0 -> 9
- net +5V: track 287.0 -> 379.6 mm, vias 6 -> 4
- net UART1_RX_LV: track 24.1 -> 113.8 mm, vias 0 -> 4
- net UART0_TX_LV: track 90.2 -> 4.17 mm
- net Net-(J13-Pad2): track 86.2 -> 5.46 mm
- net X_EN: track 80.1 -> 0.00 mm, vias 2 -> 0
- net +12P: track 138.7 -> 64.3 mm, vias 1 -> 2
- net Y_EN: track 68.4 -> 0.00 mm, vias 4 -> 0
- net Net-(JP16-Pad2): track 82.0 -> 13.6 mm
- net UART0_RX_LV: track 72.3 -> 4.17 mm, vias 3 -> 0
- net Z_EN: track 67.6 -> 0.00 mm, vias 2 -> 0
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- added copper zone on B.Cu, net +12P
- added copper zone on B.Cu, net +V_HEATBED
- added copper zone on B.Cu, net +V_MOTOR
- added copper zone on B.Cu, net +V_POWER
- added copper zone on F.Cu, net /Mosfet Outputs/D10_OUT
- added copper zone on F.Cu, net /Mosfet Outputs/D8_OUT
- added copper zone on F.Cu, net /Mosfet Outputs/D9_OUT
- added copper zone on F.Cu, net /Mosfet Outputs/FET4_OUT
- added copper zone on F.Cu, net /Power/LP_2
- added copper zone on F.Cu, net GND
- added copper zone on F.Cu, net Net-(F3-Pad2)
- added copper zone on F.Cu, net Net-(F4-Pad2)
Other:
- net class Default: clearance 0.1778 -> 0.127; trace_width 0.2032 -> 0.2; via_dia 0.635 -> 0.8; via_drill 0.3048 -> 0.3
- net class high-power: clearance 0.2032 -> 0.2; trace_width 2.286 -> 4; via_dia 2.286 -> 1; via_drill 1.016 -> 0.4
- net class low-power: clearance 0.1778 -> 0.15; trace_width 0.4064 -> 0.5; via_dia 0.635 -> 0.8; via_drill 0.3048 -> 0.3
- net class med-power: clearance 0.2032 -> 0.2; trace_width 1.143 -> 1; via_dia 1.143 -> 1; via_drill 0.508 -> 0.4
- rule trace_clearance: 0.1778 -> 0.127
- rule trace_min: 0.2032 -> 0.2
- rule via_min_drill: 0.3048 -> 0.3
- rule via_min_size: 0.635 -> 0.3
- board text added: "+5V Due"
- board text added: "+5V PSU"
- board text added: "12VIn"
- board text added: "AUX 2"
- board text added: "AUX 3"
- board text added: "AUX 4"
- board text added: "E0"
- board text added: "E1"
- board text added: "E2"
- board text added: "ENDSTOPS"
- board text added: "Emergency Stop"
- board text added: "Endstop Pullup"
- board text added: "GND"
- board text added: "I2C 0"
- board text added: "I2C 1"
- board text added: "Jumper Settings for Mode Selection"
- board text added: "RAMPS-FD v3.0 MK 2020"
- board text added: "RX"
- board text added: "Reset"
- board text added: "SPI"
- board text added: "Servos"
- board text added: "TX"
- board text added: "Thermistors"
- board text added: "UART with Address 0..3"
- board text added: "UART0"
- board text added: "UART1"
- board text added: "X"
- board text added: "X MAX"
- board text added: "X MIN"
- board text added: "Y"
- board text added: "Y MAX"
- board text added: "Y MIN"
- board text added: "Z MAX"
- board text added: "Z MIN"
- board text added: "Z1"
- board text added: "Z2"
- board text added: "uStep Resolution"
- board text removed: "MOT_IN"
- board text removed: "RAMPS-FD v2.3 bobc/MK 2019"

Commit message: Lagenspiegel, minor Silkscreen
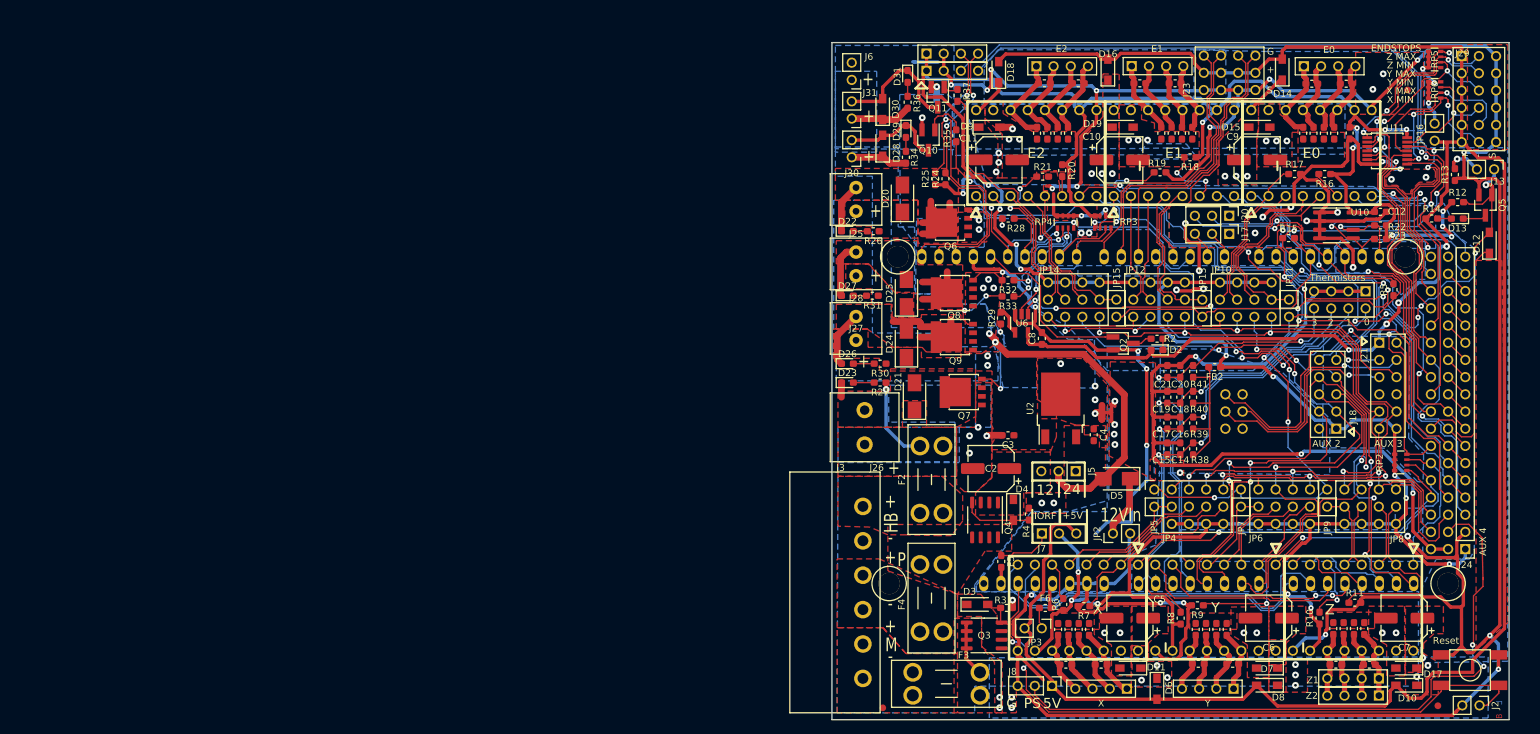
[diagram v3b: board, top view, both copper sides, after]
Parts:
- removed REF**: OSHW-Logo2_9.8x8mm_SilkScreen, Symbol:OSHW-Logo2_9.8x8mm_SilkScreen
- M2: moved to B.Cu
- moved M2 125.6 mm to (65.4, 86.6)
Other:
- board text added: "B"
- board text added: "L"
